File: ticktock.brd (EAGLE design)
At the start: 61 x 67.3 mm, 63 parts, among them IC1 ATMEGA644A, IC2 AD8611RM, IC3 REF200U, J1 AVR_SPI_PRG_6NS, Q1 MOSFET-NCHANNEL2N7002PW, Q2 MOSFET-NCHANNELBSS138, Q3 MOSFET-NCHANNELBSS138, U1 MAX232SOIC16, U2 OSCILLATORSMD, U3 FT232RLSSOP, U4 BMP180

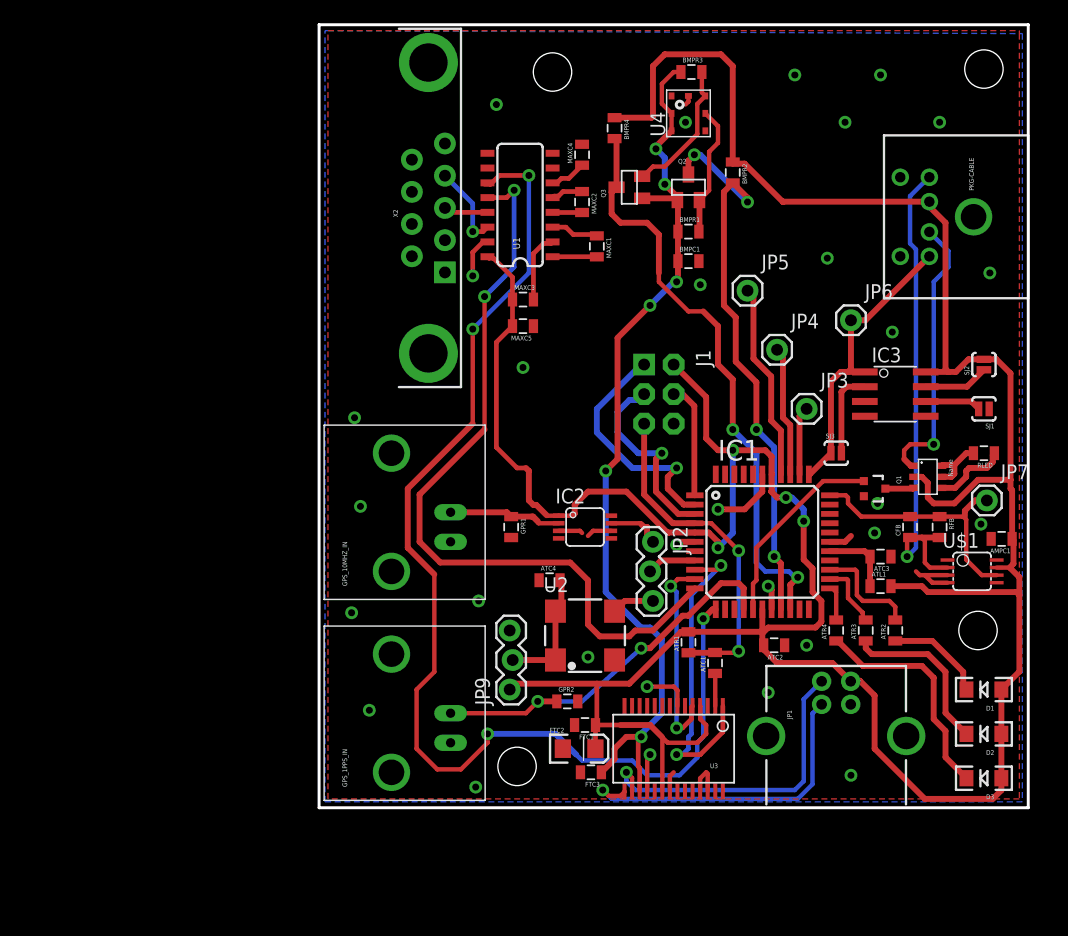
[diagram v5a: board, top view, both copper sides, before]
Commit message: Drop in BME280 (remove BMP180)
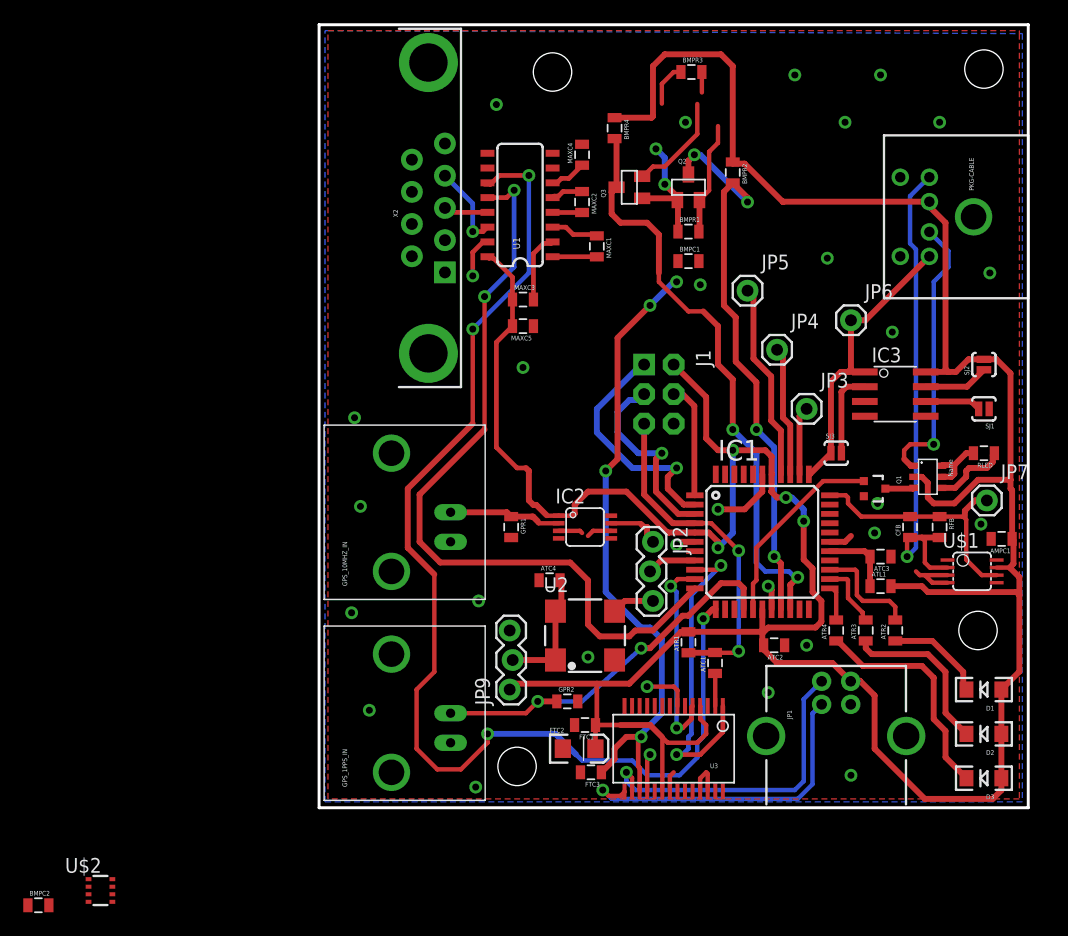
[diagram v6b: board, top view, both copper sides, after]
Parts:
- removed U4: BMP180, SparkFun-Sensors:BMP180
- added BMPC2: 100nF, SparkFun-Capacitors:0805
- added U$2: BME280BME280-LGA, tickTockLibrary:BME280
- BMPC1: value 1uF -> 100nF
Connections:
- net 3.3V: now also BMPC1.2, BMPC2.2, U$2.8; no longer BMPC1.1, U4.2, U4.3
- net GND: now also BMPC1.1, BMPC2.1, U$2.1, U$2.5, U$2.7; no longer BMPC1.2, U4.7
- net N$15: now also U$2.4; no longer U4.5
- net N$18: now also U$2.3; no longer U4.6
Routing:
- net 3.3V: track 78.9 -> 70.1 mm
- net N$15: track 11.3 -> 9.78 mm
- net N$18: track 12.0 -> 10.6 mm
- net GND: track 44.6 -> 43.8 mm
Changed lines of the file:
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@@
 <element name="AMPC1" library="SparkFun-Capacitors" package="0805" value="1uF" x="58.674" y="23.114" rot="R180"/>
 <element name="U$1" library="tickTockLibrary" package="MSOP08" value="OPA381" x="56.134" y="20.32" rot="R270"/>
-<element name="U4" library="SparkFun-Sensors" package="BMP180" value="BMP180" x="31.75" y="59.69" rot="R90"/>
 <element name="IC3" library="burr-brown" package="SO08" value="REF200U" x="49.53" y="35.56" rot="R270">
 <attribute name="OC_NEWARK" value="34C7615" x="49.53" y="35.56" size="1.778" layer="27" rot="R270" display="off"/>
@@
 <element name="BMPR3" library="SparkFun-Resistors" package="0805" value="10K" x="32.004" y="63.246"/>
 <element name="BMPR4" library="SparkFun-Resistors" package="0805" value="10K" x="25.4" y="58.42" rot="R270"/>
-<element name="BMPC1" library="SparkFun-Capacitors" package="0805" value="1uF" x="31.75" y="46.99"/>
+<element name="BMPC1" library="SparkFun-Capacitors" package="0805" value="100nF" x="31.75" y="46.99"/>
 <element name="ATR2" library="SparkFun-Resistors" package="0805" value="330" x="49.53" y="15.24" rot="R90"/>
 <element name="ATR3" library="SparkFun-Resistors" package="0805" value="330" x="46.99" y="15.24" rot="R90"/>
@@
 <element name="JP9" library="SparkFun-Connectors" package="1X03_LOCK" value="3-Pin" x="16.51" y="10.16" rot="R90"/>
 <element name="X2" library="SparkFun-Connectors" package="DB9_MALE" value="" x="9.398" y="51.562" rot="R90"/>
+<element name="U$2" library="tickTockLibrary" package="BME280" value="BME280BME280-LGA" x="-18.796" y="-7.112"/>
+<element name="BMPC2" library="SparkFun-Capacitors" package="0805" value="100nF" x="-24.13" y="-8.382"/>
 </elements>
 <signals>
@@
 <contactref element="PKG-CABLE" pad="5"/>
 <contactref element="SJ1" pad="1"/>
-<contactref element="U4" pad="7"/>
-<contactref element="BMPC1" pad="2"/>
 <contactref element="PKG-CABLE" pad="6"/>
 <contactref element="U$1" pad="3"/>
@@
 </polygon>
 <via x="32.766" y="44.958" extent="1-16" drill="0.6"/>
-<wire x1="31.75" y1="61.19" x2="31.75" y2="60.706" width="0.381" layer="1"/>
 <via x="31.496" y="58.928" extent="1-16" drill="0.6"/>
 <via x="40.894" y="62.992" extent="1-16" drill="0.6"/>
@@
 <wire x1="30.48" y1="10.414" x2="28.194" y2="10.414" width="0.381" layer="1"/>
 <via x="28.194" y="10.414" extent="1-16" drill="0.6"/>
-<wire x1="31.75" y1="60.706" x2="31.496" y2="60.452" width="0.381" layer="1"/>
 <via x="13.208" y="45.72" extent="1-16" drill="0.6"/>
 <wire x1="14.472" y1="48.641" x2="14.097" y2="48.641" width="0.4064" layer="1"/>
@@
 <wire x1="13.208" y1="47.752" x2="13.208" y2="45.72" width="0.4064" layer="1"/>
 <contactref element="X2" pad="5"/>
+<contactref element="U$2" pad="1"/>
+<contactref element="U$2" pad="7"/>
+<contactref element="BMPC2" pad="1"/>
+<contactref element="BMPC1" pad="1"/>
+<contactref element="U$2" pad="5"/>
+<wire x1="32.766" y1="44.958" x2="30.85" y2="46.99" width="0" layer="19" extent="1-1"/>
 <wire x1="28.205" y1="1.424" x2="30.155" y2="1.424" width="0" layer="19" extent="1-1"/>
+<wire x1="-17.771" y1="-6.137" x2="4.318" y2="8.382" width="0" layer="19" extent="1-1"/>
+<wire x1="-19.821" y1="-6.787" x2="-17.771" y2="-6.137" width="0" layer="19" extent="1-1"/>
+<wire x1="-19.821" y1="-8.087" x2="-19.821" y2="-6.787" width="0" layer="19" extent="1-1"/>
+<wire x1="-25.03" y1="-8.382" x2="-19.821" y2="-8.087" width="0" layer="19" extent="1-1"/>
 </signal>
 <signal name="IR_PWM">
@@
 <contactref element="FTC3" pad="1"/>
 <contactref element="BMPR3" pad="1"/>
-<contactref element="U4" pad="2"/>
-<contactref element="U4" pad="3"/>
-<contactref element="BMPC1" pad="1"/>
 <contactref element="Q2" pad="1"/>
 <contactref element="Q3" pad="1"/>
@@
 <wire x1="30.8" y1="52.24" x2="30.65" y2="52.39" width="0.508" layer="1"/>
 <wire x1="30.65" y1="52.39" x2="27.77" y2="52.39" width="0.508" layer="1"/>
-<wire x1="30.3" y1="59.69" x2="30.3" y2="58.19" width="0.381" layer="1"/>
-<wire x1="30.3" y1="59.69" x2="29.464" y2="60.526" width="0.381" layer="1"/>
 <wire x1="29.464" y1="60.526" x2="29.464" y2="62.23" width="0.381" layer="1"/>
 <wire x1="29.464" y1="62.23" x2="30.48" y2="63.246" width="0.381" layer="1"/>
@@
 <via x="28.956" y="56.642" extent="1-16" drill="0.6"/>
 <wire x1="28.956" y1="56.642" x2="28.956" y2="56.846" width="0.508" layer="1"/>
-<wire x1="28.956" y1="56.846" x2="30.3" y2="58.19" width="0.508" layer="1"/>
-<wire x1="30.85" y1="46.99" x2="30.85" y2="45.328" width="0.508" layer="1"/>
 <wire x1="30.85" y1="45.328" x2="30.734" y2="45.212" width="0.508" layer="1"/>
 <via x="30.734" y="45.212" extent="1-16" drill="0.6"/>
@@
 <wire x1="30.85" y1="49.53" x2="30.85" y2="52.19" width="0.508" layer="1"/>
 <wire x1="30.85" y1="52.19" x2="30.8" y2="52.24" width="0.508" layer="1"/>
-<wire x1="30.85" y1="49.53" x2="30.85" y2="46.99" width="0.508" layer="1"/>
 <wire x1="28.448" y1="43.18" x2="25.654" y2="40.386" width="0.508" layer="1"/>
 <wire x1="25.654" y1="40.386" x2="25.654" y2="29.972" width="0.508" layer="1"/>
@@
 <wire x1="27.432" y1="3.556" x2="27.555" y2="3.433" width="0.4064" layer="1"/>
 <wire x1="27.555" y1="3.433" x2="27.555" y2="1.424" width="0.4064" layer="1"/>
+<contactref element="U$2" pad="8"/>
+<contactref element="BMPC1" pad="2"/>
+<contactref element="BMPC2" pad="2"/>
+<wire x1="28.956" y1="56.846" x2="29.464" y2="60.526" width="0" layer="19" extent="1-1"/>
+<wire x1="32.65" y1="46.99" x2="30.85" y2="49.53" width="0" layer="19" extent="1-1"/>
+<wire x1="30.85" y1="45.328" x2="32.65" y2="46.99" width="0" layer="19" extent="1-1"/>
+<wire x1="-19.821" y1="-6.137" x2="24.268" y2="3.048" width="0" layer="19" extent="1-1"/>
+<wire x1="-23.23" y1="-8.382" x2="-19.821" y2="-6.137" width="0" layer="19" extent="1-1"/>
 </signal>
 <signal name="USB_DTR">
@@
 <contactref element="BMPR1" pad="2"/>
 <contactref element="Q2" pad="2"/>
-<contactref element="U4" pad="5"/>
 <wire x1="32.65" y1="49.53" x2="32.7" y2="49.53" width="0.4064" layer="1"/>
 <wire x1="32.7" y1="49.53" x2="32.7" y2="52.24" width="0.508" layer="1"/>
@@
 <wire x1="33.528" y1="56.388" x2="34.29" y2="57.15" width="0.381" layer="1"/>
 <wire x1="34.29" y1="57.15" x2="34.29" y2="58.6" width="0.381" layer="1"/>
-<wire x1="34.29" y1="58.6" x2="33.2" y2="59.69" width="0.381" layer="1"/>
+<contactref element="U$2" pad="4"/>
+<wire x1="-17.771" y1="-8.087" x2="32.65" y2="49.53" width="0" layer="19" extent="1-1"/>
 </signal>
 <signal name="I2C_SCL">
@@
 <contactref element="BMPR3" pad="2"/>
 <contactref element="Q3" pad="2"/>
-<contactref element="U4" pad="6"/>
 <wire x1="32.512" y1="57.912" x2="29.718" y2="55.118" width="0.381" layer="1"/>
 <wire x1="29.718" y1="55.118" x2="28.702" y2="55.118" width="0.381" layer="1"/>
 <wire x1="28.702" y1="55.118" x2="27.874" y2="54.29" width="0.381" layer="1"/>
 <wire x1="27.874" y1="54.29" x2="27.77" y2="54.29" width="0.381" layer="1"/>
-<wire x1="33.2" y1="61.19" x2="32.904" y2="61.486" width="0.381" layer="1"/>
 <wire x1="32.904" y1="61.486" x2="32.904" y2="63.246" width="0.381" layer="1"/>
-<wire x1="33.2" y1="61.19" x2="32.512" y2="60.502" width="0.381" layer="1"/>
 <wire x1="32.512" y1="60.502" x2="32.512" y2="57.912" width="0.381" layer="1"/>
+<contactref element="U$2" pad="3"/>
+<wire x1="32.512" y1="60.502" x2="32.904" y2="61.486" width="0" layer="19" extent="1-1"/>
+<wire x1="-17.771" y1="-7.437" x2="27.77" y2="54.29" width="0" layer="19" extent="1-1"/>
 </signal>
 <signal name="I2C_SDA">

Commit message: Place new BME280 and old BMP180 on board
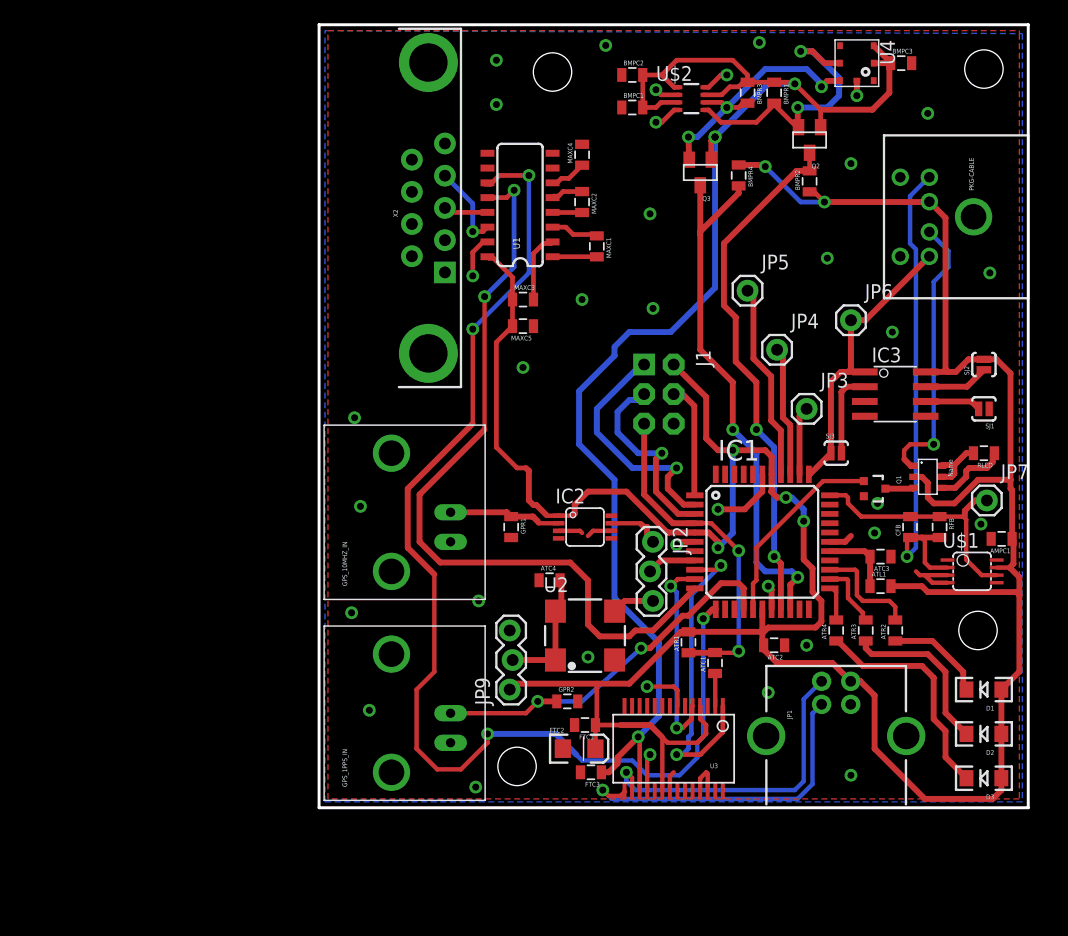
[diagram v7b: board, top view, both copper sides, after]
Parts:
- added BMPC3: 1uF, SparkFun-Capacitors:0805
- added U4: BMP180, SparkFun-Sensors:BMP180
- moved BMPC2 87.8 mm to (26.9, 63.0)
- moved U$2 84.9 mm to (32.0, 61.0)
- moved BMPC1 14.1 mm to (26.9, 60.2)
- moved BMPR1 14.0 mm to (39.1, 61.5), turned to 270 degrees
- moved BMPR4 11.4 mm to (36.1, 54.4)
- moved Q2 11.2 mm to (42.2, 57.4), turned to 180 degrees
- moved BMPR2 6.65 mm to (42.2, 53.8), turned to 90 degrees
- moved Q3 6.23 mm to (32.8, 54.6), turned to 180 degrees
- moved BMPR3 5.14 mm to (36.8, 61.5), turned to 270 degrees
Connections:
- removed net N$18: BMPR3.2, Q3.2, U$2.3
- new net N$23: BMPR3.2, Q3.2, U$2.3, U4.6
- net 3.3V: now also BMPC3.1, U$2.2, U$2.6, U4.2, U4.3
- net GND: now also BMPC3.2, U4.7
- net N$15: now also U4.5
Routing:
- net 3.3V: track 70.1 -> 126.7 mm, vias 6 -> 4
- net N$23: track 0.00 -> 22.7 mm, vias 0 -> 3
- net 5V: track 295.3 -> 272.7 mm, vias 4 -> 6
- net N$15: track 9.78 -> 25.5 mm, vias 0 -> 2
- net N$18: track 10.6 -> 1.27 mm, vias 0 -> 1
- net GND: track 43.8 -> 50.9 mm, vias 30 -> 35
- net I2C_SCL: track 49.3 -> 45.0 mm, vias 4 -> 2
- net I2C_SDA: track 51.0 -> 47.1 mm

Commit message: Clean up DRC errors
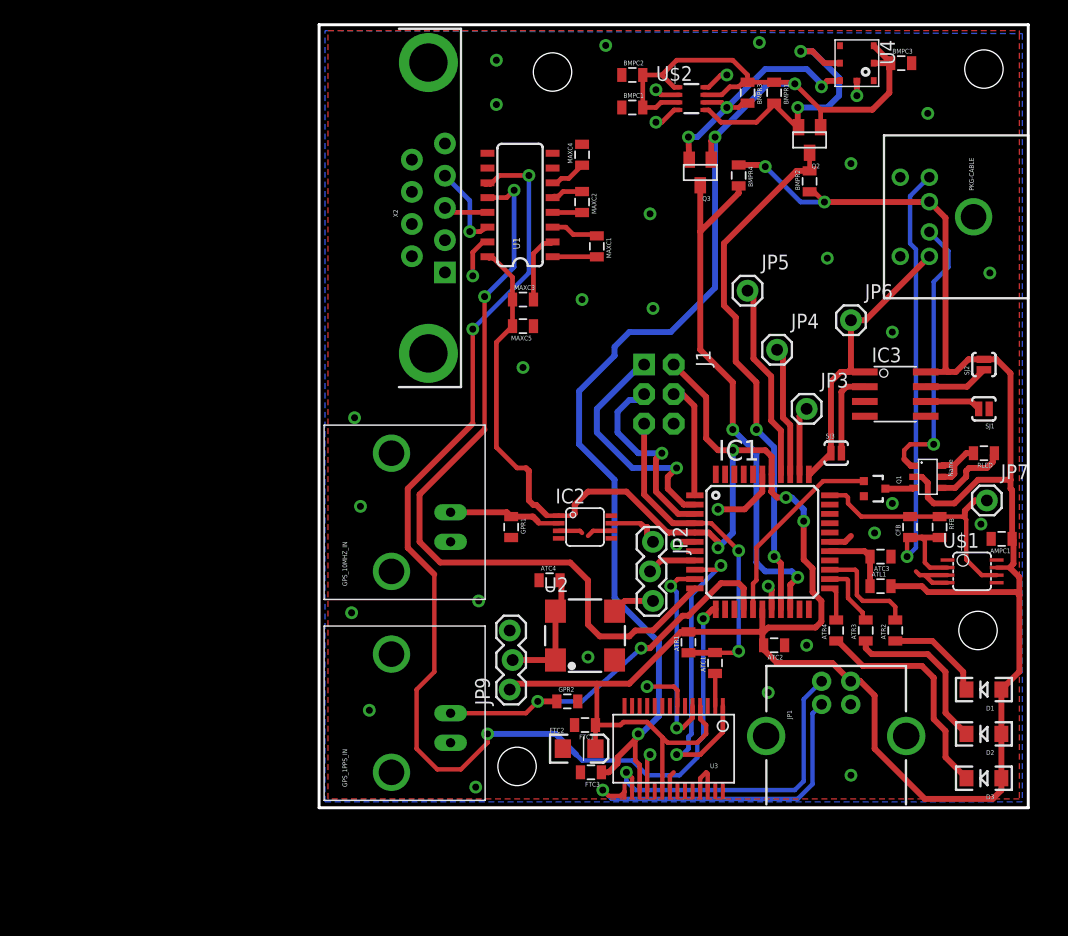
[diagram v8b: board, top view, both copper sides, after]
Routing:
- net GND: track 50.9 -> 52.2 mm, vias 35 -> 36
- net N$18: track 1.27 -> 0.00 mm, vias 1 -> 0
- net 3.3V: track 126.7 -> 126.9 mm, vias 4 -> 3
